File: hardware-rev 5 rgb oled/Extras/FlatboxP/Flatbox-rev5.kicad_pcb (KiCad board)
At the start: 2 copper layers, 210 x 120 mm, 40 parts, among them SW10 SW_Push, SW11 SW_Push, SW12 SW_Push, SW13 SW_Push, SW14 SW_Push, SW15 SW_Push, SW16 SW_Push, SW17 SW_Push, SW18 SW_Push, SW7 SW_Push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

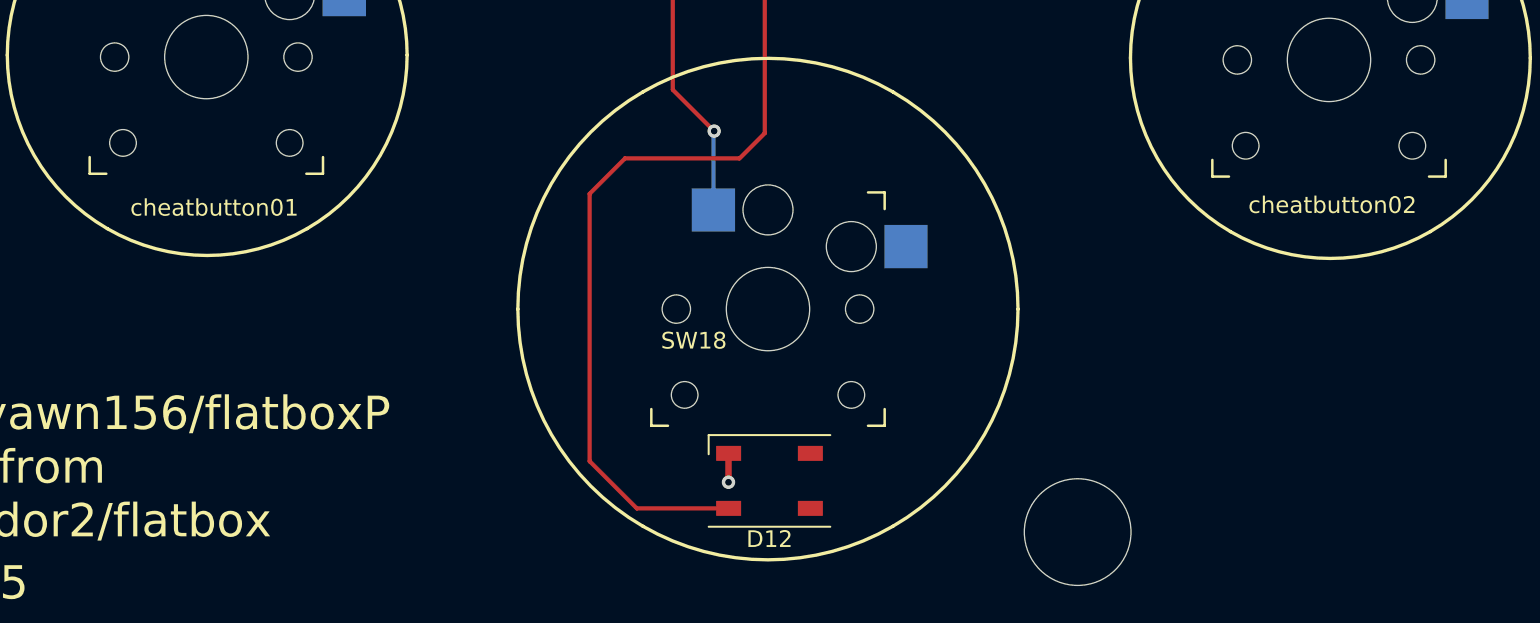
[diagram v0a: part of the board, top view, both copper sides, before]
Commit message: Added LEDs to cheatbutton01 and cheatbutton02
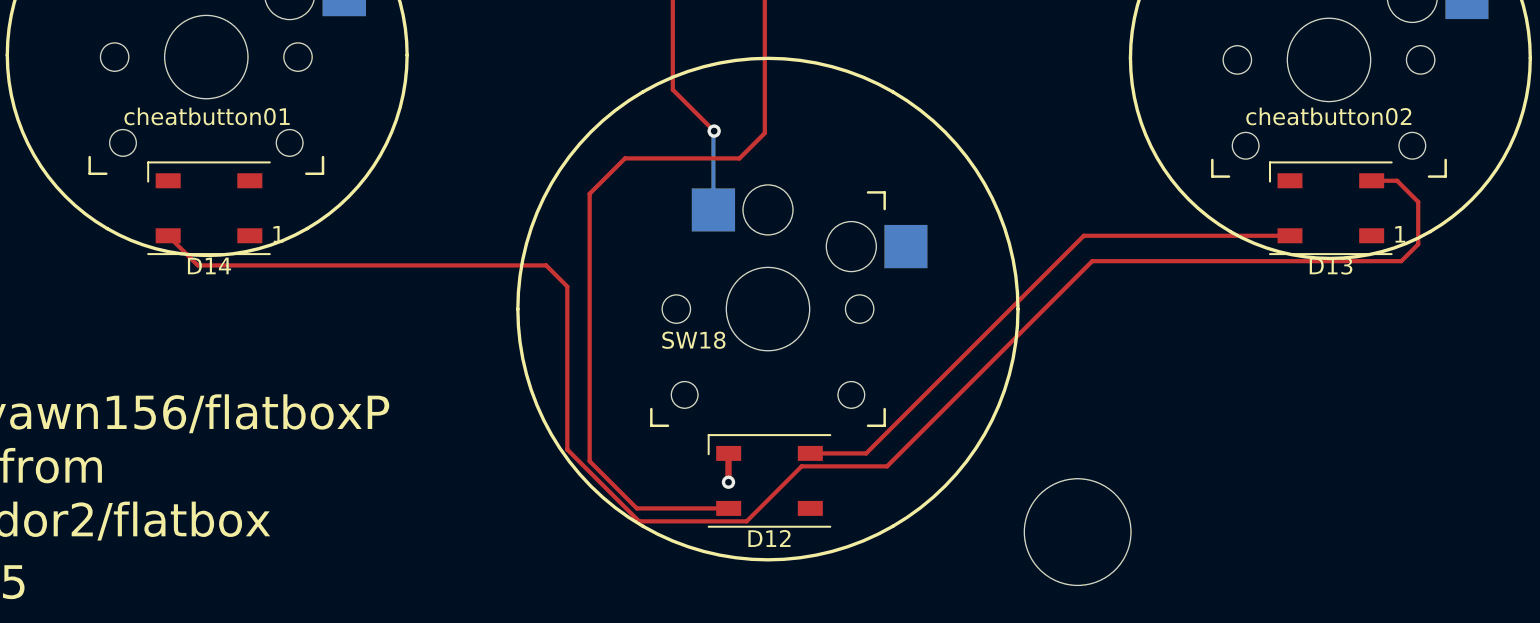
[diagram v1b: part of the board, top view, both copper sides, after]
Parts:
- added D13: WS2812B, LED_SMD:LED_WS2812B_PLCC4_5.0x5.0mm_P3.2mm, F.Cu at (165.2, 123.6)
- added D14: WS2812B, LED_SMD:LED_WS2812B_PLCC4_5.0x5.0mm_P3.2mm, F.Cu at (97.9, 123.6)
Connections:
- D12 pad 2: unconnected-(D12-DOUT-Pad2) -> LED13
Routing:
- net LED14: track 0.00 -> 100.8 mm
- net LED13: track 0.00 -> 34.2 mm
